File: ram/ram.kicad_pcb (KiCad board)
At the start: 4 copper layers, 102.4 x 40.3 mm, 7 parts, among them J2 Conn_01x03, U1 IS66WVE4M16EBLL-70BLI, U3 74LVC2G00

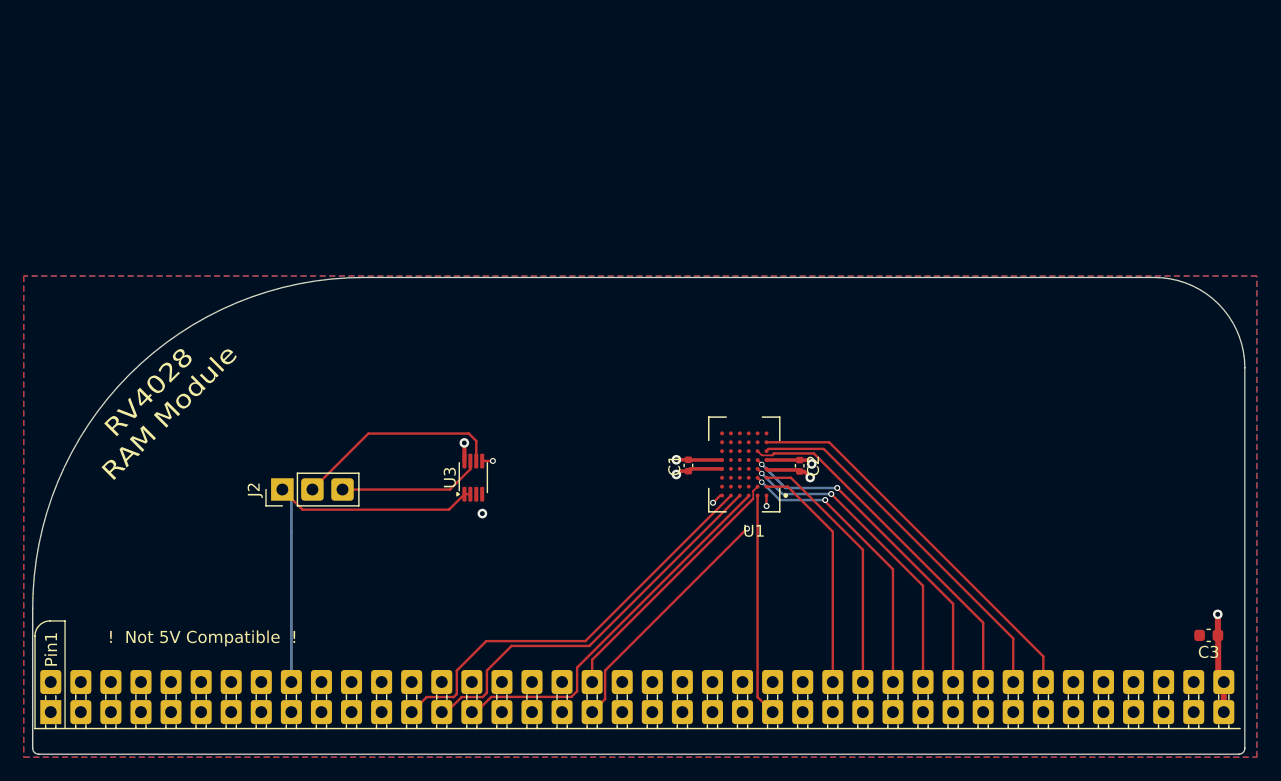
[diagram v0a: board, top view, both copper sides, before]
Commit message: BGA layout is a pain
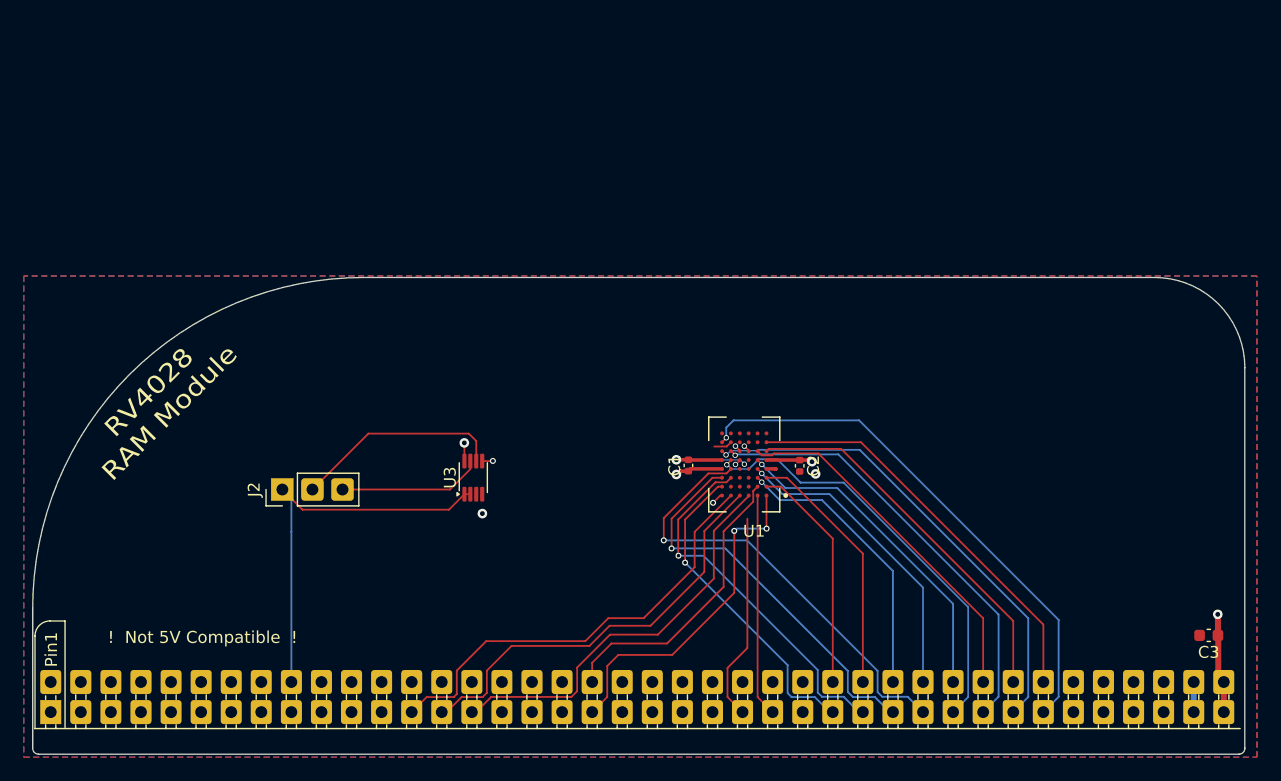
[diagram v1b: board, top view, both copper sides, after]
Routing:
- net /D7: track 0.00 -> 45.0 mm, vias 0 -> 1
- net /D6: track 0.00 -> 40.6 mm, vias 0 -> 1
- net /D3: track 0.00 -> 38.2 mm, vias 0 -> 1
- net /D5: track 0.00 -> 37.0 mm, vias 0 -> 1
- net /D4: track 0.00 -> 35.9 mm, vias 0 -> 1
- net /D2: track 0.00 -> 33.7 mm, vias 0 -> 1
- net /D1: track 0.00 -> 31.1 mm, vias 0 -> 1
- net /D0: track 0.00 -> 27.0 mm, vias 0 -> 1
- net /~{WE}: track 0.00 -> 19.1 mm
- net /~{LB}: track 21.8 -> 28.5 mm
- net /~{UB}: track 22.3 -> 25.0 mm
- net /A1: track 32.1 -> 34.5 mm
- net /A22: track 0.00 -> 2.34 mm, vias 0 -> 1
- net /A2: track 33.8 -> 35.9 mm
- net GND: track 7.86 -> 9.75 mm
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
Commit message: RAM board attempt 2
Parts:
- added C5: 100n, Capacitor_SMD:C_0402_1005Metric, F.Cu at (120.0, 67.0)
- added J3: Conn_01x03, Connector_PinHeader_2.54mm:PinHeader_1x03_P2.54mm_Vertical, F.Cu at (105.0, 76.5)
- added U2: 74LVC32, Package_SO:SSOP-14_5.3x6.2mm_P0.65mm, F.Cu at (116.0, 71.0)
- J1: footprint RV4028:ModuleHeader -> RV4028:Module_2mm
- U3: value 74LVC2G00 -> 74LVC2G04; footprint Package_SO:VSSOP-8_2.3x2mm_P0.5mm -> Package_TO_SOT_SMD:SOT-363_SC-70-6
- moved C3 58.0 mm to (144.1, 69.5), turned to 0 degrees
- moved C1 25.3 mm to (128.4, 74.8), turned to 180 degrees
- moved C2 25.1 mm to (139.9, 74.0), turned to 0 degrees
- moved U1 25.0 mm to (134.4, 74.4)
- moved J2 23.1 mm to (109.0, 76.5), turned to 0 degrees
- moved J1 22.3 mm to (132.0, 95.8)
- moved U3 20.2 mm to (105.0, 87.0), turned to 0 degrees
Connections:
- J1 pad 18: unconnected-(J1-PWR-Pad18) -> +3V3
- J1 pad 23: unconnected-(J1-~{REQ}-Pad23) -> /~{REQ}
- J1 pad 40: +3V3 -> unconnected-(J1-+5V-Pad40)
- J1 pad 48: unconnected-(J1-A24-Pad48) -> /A24
- J1 pad 58: unconnected-(J1-PWR-Pad58) -> +3V3
- J1 pad 60: unconnected-(J1-~{RST2}-Pad60) -> GND
- J1 pad 61: unconnected-(J1-CLK2-Pad61) -> GND
- J1 pad 63: /LO_ADDR -> /~{LO_ADDR}
- J1 pad 66: unconnected-(J1-SPARE1-Pad66) -> GND
- J1 pad 80: +3V3 -> unconnected-(J1-+5V-Pad80)
- U3 pad 2: /A23 -> GND
- U3 pad 3: /~{CE} -> /A24
- U3 pad 4: GND -> /~{A24}
- U3 pad 5: /LO_ADDR -> +3V3
- U3 pad 6: Net-(J2-Pin_2) -> /~{A23}
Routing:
- net /A15: track 0.58 -> 59.1 mm
- net /A8: track 0.00 -> 42.1 mm, vias 0 -> 1
- net /A7: track 0.00 -> 35.5 mm, vias 0 -> 2
- net /A6: track 0.00 -> 34.6 mm, vias 0 -> 2
- net /A4: track 0.00 -> 33.2 mm
- net /A23: track 32.6 -> 0.00 mm
- net /A5: track 0.00 -> 32.4 mm
- net /A18: track 0.00 -> 29.8 mm, vias 0 -> 1
- net /A16: track 0.58 -> 26.4 mm
- net /A17: track 0.54 -> 26.1 mm
- net Net-(J2-Pin_2): track 17.7 -> 0.00 mm
- net /~{A23}: track 12.2 -> 0.00 mm
- net +3V3: track 19.0 -> 8.54 mm, vias 5 -> 3
- net /A3: track 37.4 -> 27.8 mm, vias 0 -> 1
- net /~{WE}: track 19.1 -> 28.7 mm, vias 0 -> 2
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- removed copper zone on B.Cu, net GND
- removed copper zone on F.Cu, net GND
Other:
- board size 102.4 x 40.3 mm -> 84 x 40 mm
- board text removed: "! Not 5V Compatible !"
- board text removed: "RV4028 RAM"
- board text removed: "RV4028 RAM Module"

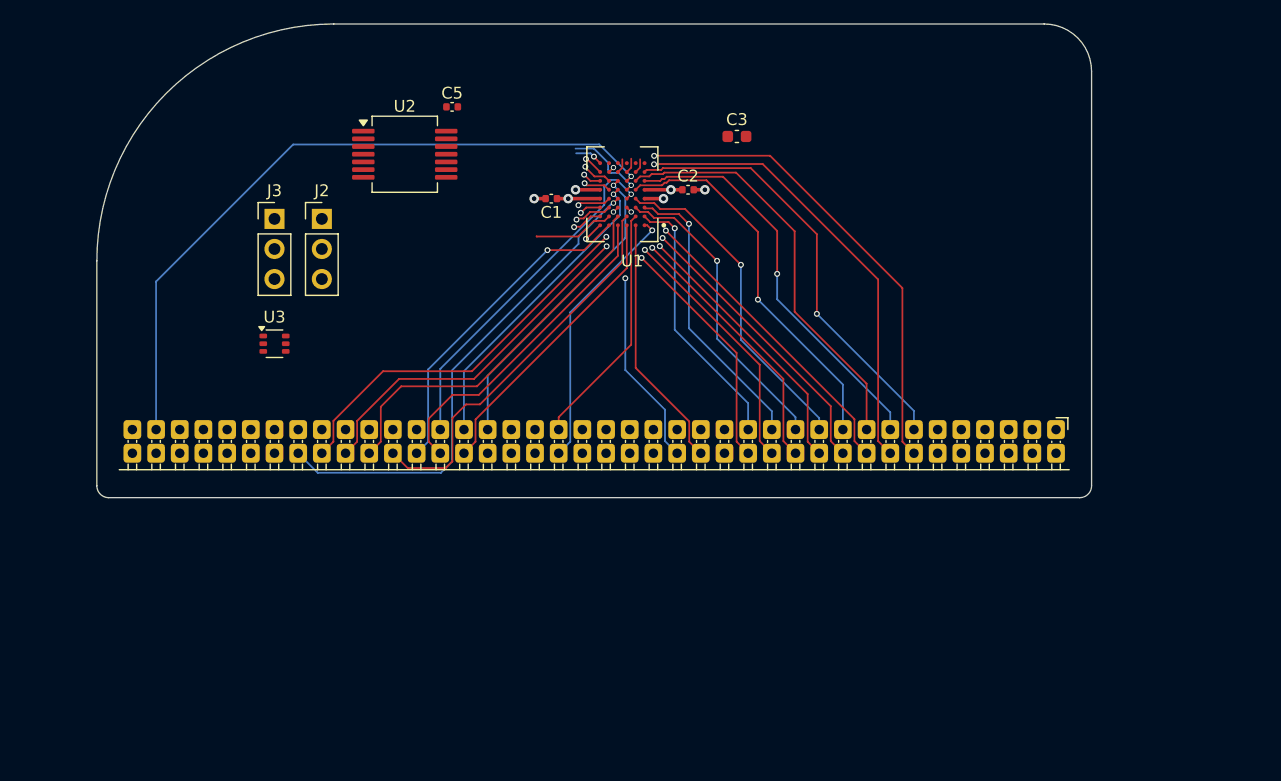
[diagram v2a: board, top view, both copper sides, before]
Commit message: Finish RAM module routing
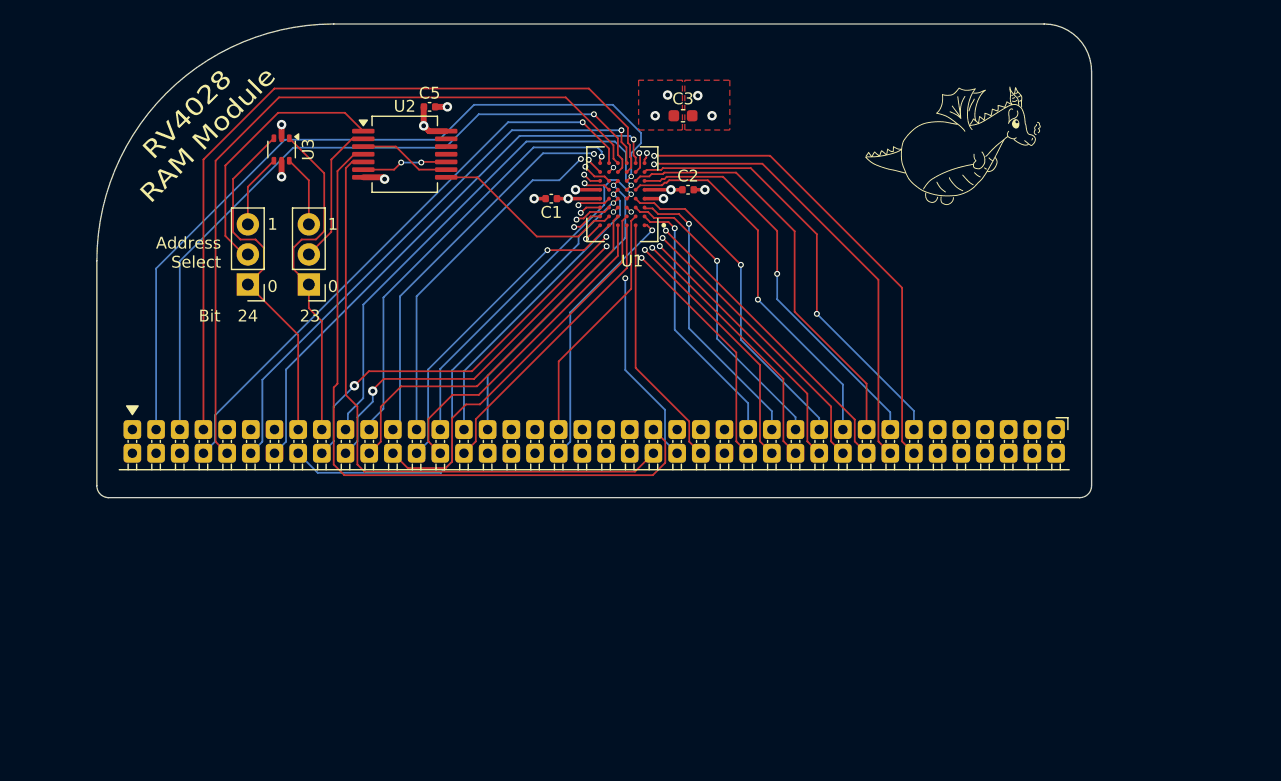
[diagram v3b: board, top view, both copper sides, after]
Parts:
- moved U3 16.4 mm to (105.6, 70.6), turned to -90 degrees
- moved J3 5.98 mm to (102.8, 82.0), turned to 180 degrees
- moved J2 5.65 mm to (107.9, 82.0), turned to 180 degrees
- moved C3 4.87 mm to (139.5, 67.8)
- moved C5 1.90 mm to (118.1, 67.0)
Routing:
- net /A13: track 1.28 -> 66.5 mm
- net /A11: track 0.00 -> 64.3 mm
- net /~{LO_ADDR}: track 0.00 -> 59.7 mm
- net /A14: track 1.23 -> 60.4 mm, vias 0 -> 1
- net /~{REQ}: track 0.00 -> 53.0 mm
- net /A12: track 0.00 -> 49.3 mm, vias 0 -> 1
- net /A10: track 0.00 -> 48.6 mm, vias 0 -> 1
- net /A9: track 0.00 -> 47.2 mm, vias 0 -> 1
- net /A20: track 1.23 -> 38.7 mm, vias 0 -> 2
- net /A19: track 0.00 -> 37.1 mm, vias 0 -> 2
- net /A22: track 6.86 -> 42.9 mm
- net /A21: track 2.38 -> 36.5 mm
- net /A24: track 0.00 -> 30.2 mm
- net /A23: track 0.00 -> 28.6 mm
- net Net-(J3-Pin_2): track 0.00 -> 22.6 mm
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- added copper zone on F.Cu, net +3V3
- added copper zone on F.Cu, net GND
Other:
- board text added: "0"
- board text added: "1"
- board text added: "23"
- board text added: "24"
- board text added: "Address Select"
- board text added: "Bit"
- board text added: "RV4028 RAM"
- board text added: "RV4028 RAM Module"

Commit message: Pull up on REQ
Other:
- board text added: "RV2048 RAM v0.1 © Michael Bell 2026 JLCJLCJLCJLC"
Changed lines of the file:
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@@
 			)
 		)
+		(property "JLC" "C1350157"
+			(at 0 0 180)
+			(unlocked yes)
+			(layer "F.Fab")
+			(hide yes)
+			(effects
+				(font
+					(size 1 1)
+					(thickness 0.15)
+				)
+			)
+		)
 		(sheetname "/")
 		(sheetfile "ram.kicad_sch")
@@
 		)
 	)
+	(gr_text "RV2048 RAM v0.1\n© Michael Bell 2026\nJLCJLCJLCJLC"
+		(at 173 80 90)
+		(layer "B.SilkS")
+		(effects
+			(font
+				(size 1 1)
+				(thickness 0.1)
+			)
+			(justify bottom mirror)
+		)
+	)
